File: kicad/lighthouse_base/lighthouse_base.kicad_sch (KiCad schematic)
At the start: 2 parts, among them J1 USB_C_Receptacle_USB2.0_14P, U1 NINA-B312

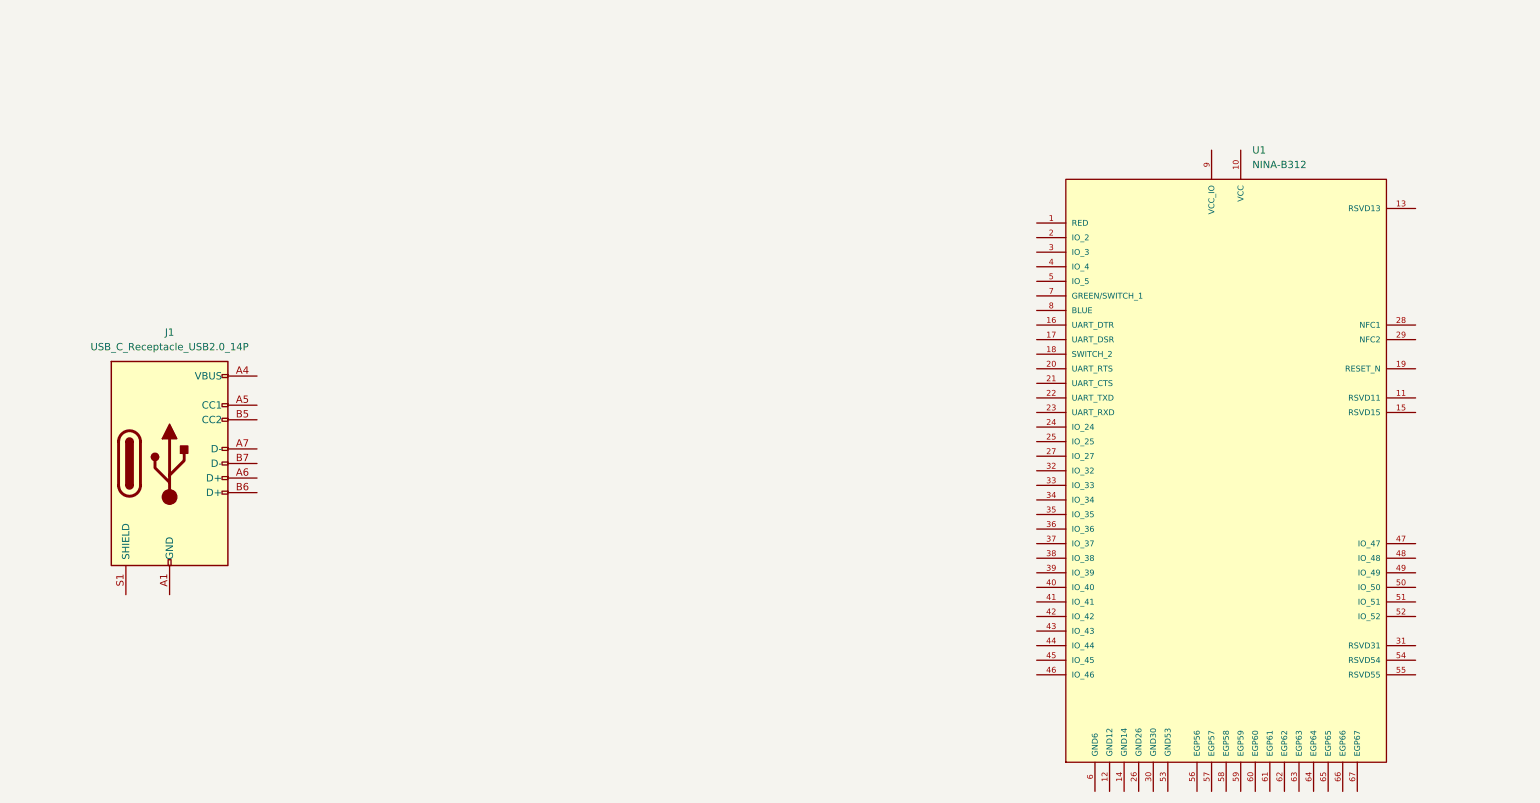
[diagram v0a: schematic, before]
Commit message: added sheets for mcu and peripherials
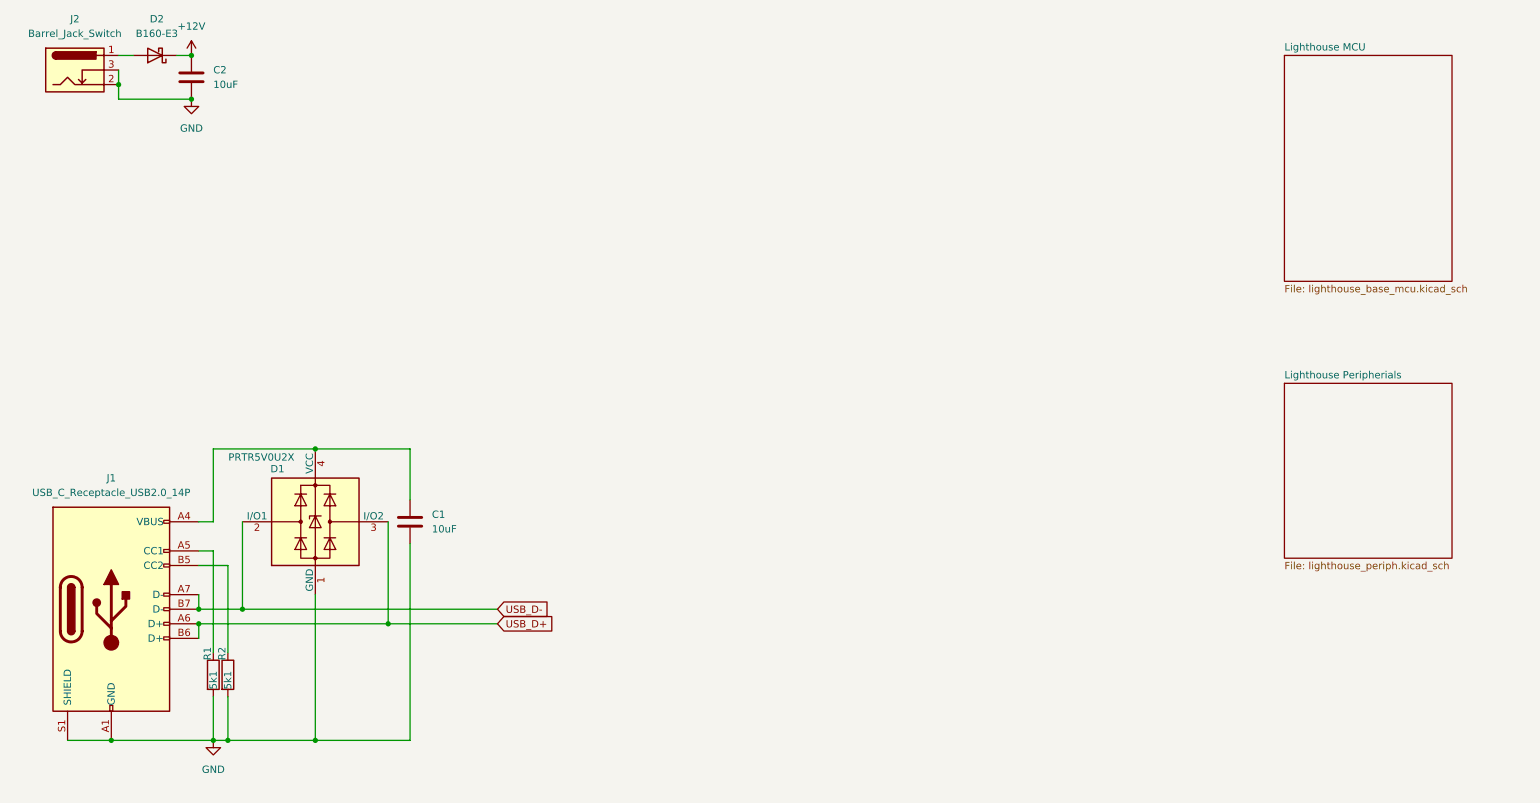
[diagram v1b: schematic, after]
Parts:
- removed U1: NINA-B312, NINA-B312:NINA_LGA67R_1500X1000X338_PIFA, symbol NINA-B312:NINA-B312
- added C1, C2: 10uF, symbol Device:C
- added D1: PRTR5V0U2X, Package_TO_SOT_SMD:SOT-143, symbol Power_Protection:PRTR5V0U2X
- added D2: B160-E3, Diode_SMD:D_SMA, symbol Diode:B160-E3
- added J2: Barrel_Jack_Switch, symbol Connector:Barrel_Jack_Switch
- added R1, R2: 5k1, symbol Device:R
- J1: footprint (none) -> Connector_USB:USB_C_Receptacle_GCT_USB4110
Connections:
- net GND: now reaches J1.A1 (GND), J1.A12 (GND), J1.B1 (GND), J1.B12 (GND)
- net GND: now also J1.S1 (SHIELD), C1.2, C2.2, D1.1 (GND), J2.2, J2.3, R1.2, R2.2
- net at J1.A4 (VBUS), J1.A9 (VBUS), J1.B4 (VBUS)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: now also C1.1, D1.4 (VCC)
- net at J1.A5 (CC1): now also R1.1
- net USB_D+: now reaches J1.A6 (D+)
- net USB_D+: now also J1.B6 (D+), D1.3 (I/O2)
- net USB_D-: now reaches J1.A7 (D-)
- net USB_D-: now also J1.B7 (D-), D1.2 (I/O1)
- net at J1.B5 (CC2): now also R2.1
- new net: D2.2 (A), J2.1
- new net +12V: C2.1, D2.1 (K)
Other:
- added sheet Lighthouse MCU (lighthouse_base_mcu.kicad_sch)
- added sheet Lighthouse Peripherials (lighthouse_periph.kicad_sch)
- moved on the sheet: J1

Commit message: schema v1 done
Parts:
- removed D2: B160-E3, Diode_SMD:D_SMA, symbol Diode:B160-E3
- added C11, C12, C13: 10uF, symbol Device:C
- added D2, D3: B130-13-F, symbol Device:D_Schottky
- added D4: DF2S16FS, Diode_SMD:D_SOD-523, symbol Diode:ESD5Zxx
- added Q1: PMOS, symbol Simulation_SPICE:PMOS
- added R7, R8: 22R, symbol Device:R
- added U6: R-78E5.0-1.0, Converter_DCDC:Converter_DCDC_RECOM_R-78E-0.5_THT, symbol Regulator_Switching:R-78E5.0-1.0
- added U7: TLV75533PDBV, Package_TO_SOT_SMD:SOT-23-5, symbol Regulator_Linear:TLV75533PDBV
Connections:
- net +12V: now also Q1.3 (S), U6.1 (IN)
- net GND: now also C11.2, C12.2, C13.2, D4.2 (A), Q1.2 (G), U6.2 (GND), U7.2 (GND)
- net USB_D+: now also R8.2; no longer D1.3 (I/O2), J1.A6 (D+), J1.B6 (D+)
- net USB_D-: now also R7.2; no longer D1.2 (I/O1), J1.A7 (D-), J1.B7 (D-)
- net VBUS: now reaches C1.1, D1.4 (VCC), J1.A4 (VBUS), J1.A9 (VBUS), J1.B4 (VBUS), J1.B9 (VBUS)
- net VBUS: now also D2.2 (A)
- net at J2.1: now also D4.1 (K), Q1.1 (D)
- new net: D1.3 (I/O2), J1.A6 (D+), J1.B6 (D+), R8.1
- new net: D1.2 (I/O1), J1.A7 (D-), J1.B7 (D-), R7.1
- new net: C12.1, D3.2 (A), U6.3 (OUT)
- new net +3.3V: C13.1, U7.5 (OUT)
- new net +5V: C11.1, D2.1 (K), D3.1 (K), U7.1 (IN), U7.3 (EN)
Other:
- note added: "R-78K5.0-0.5 R-78E5.0-1.0"
- moved on the sheet: C1, C2, D1, J1, J2, R1, R2

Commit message: schematics done
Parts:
- added BT1: Battery_Cell, Connector_PinHeader_2.54mm:PinHeader_1x02_P2.54mm_Vertical, symbol Device:Battery_Cell
- added C6: 10nF, Capacitor_SMD:C_0201_0603Metric_Pad0.64x0.40mm_HandSolder, symbol Device:C
- added R1: 1M, Resistor_SMD:R_0603_1608Metric_Pad0.98x0.95mm_HandSolder, symbol Device:R
- added R2: 10k, Resistor_SMD:R_0603_1608Metric_Pad0.98x0.95mm_HandSolder, symbol Device:R
- added U2: MCP73831-2-OT, Package_TO_SOT_SMD:SOT-23-5, symbol Battery_Management:MCP73831-2-OT
- added U4: MCP111T-xxxE_TT, Package_TO_SOT_SMD:SOT-23-3, symbol MEgliParts:MCP111T-xxxE_TT
- C1: renamed from C2; footprint (none) -> Capacitor_SMD:C_0805_2012Metric_Pad1.18x1.45mm_HandSolder
- C2: renamed from C12; footprint (none) -> Capacitor_SMD:C_0805_2012Metric_Pad1.18x1.45mm_HandSolder
- C3: renamed from C11; footprint (none) -> Capacitor_SMD:C_0805_2012Metric_Pad1.18x1.45mm_HandSolder
- C4: renamed from C13; footprint (none) -> Capacitor_SMD:C_0805_2012Metric_Pad1.18x1.45mm_HandSolder
- C5: renamed from C1; footprint (none) -> Capacitor_SMD:C_0805_2012Metric_Pad1.18x1.45mm_HandSolder
- D1: renamed from D3; footprint (none) -> Diode_SMD:D_SMA_Handsoldering
- D3: renamed from D2; footprint (none) -> Diode_SMD:D_SMA_Handsoldering
- Q1: footprint (none) -> Package_TO_SOT_SMD:SOT-23
- R3: renamed from R7; footprint (none) -> Resistor_SMD:R_0603_1608Metric_Pad0.98x0.95mm_HandSolder
- R4: renamed from R8; footprint (none) -> Resistor_SMD:R_0603_1608Metric_Pad0.98x0.95mm_HandSolder
- R5: renamed from R1; footprint (none) -> Resistor_SMD:R_0603_1608Metric_Pad0.98x0.95mm_HandSolder
- R6: renamed from R2; footprint (none) -> Resistor_SMD:R_0603_1608Metric_Pad0.98x0.95mm_HandSolder
- renumbered D4 to D2, D1 to D4, J2 to J1, J1 to J2, U6 to U1, U7 to U3
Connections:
- net +5V: now also U2.4 (V_{DD}); no longer U3.1 (IN), U3.3 (EN)
- net GND: now also BT1.2 (-), C6.2, R2.2, U2.2 (V_{SS}), U4.2 (VSS)
- new net: C6.1, R1.2, U3.3 (EN), U4.1 (VOUT)
- new net: R2.1, U2.5 (PROG)
- new net +BATT: BT1.1 (+), R1.1, U2.3 (V_{BAT}), U3.1 (IN), U4.3 (VDD)
- new net CH_STAT: U2.1 (STAT)
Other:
- moved on the sheet: C3, C4, U3

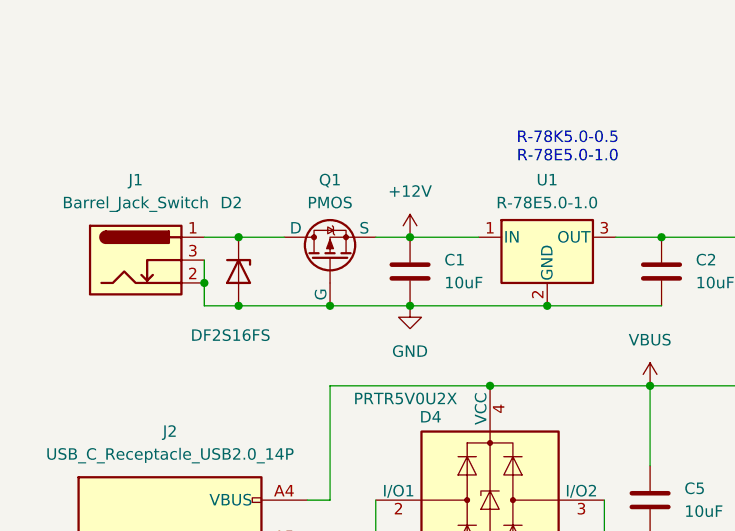
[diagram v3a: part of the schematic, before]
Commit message: started with pcb lighthouse_base
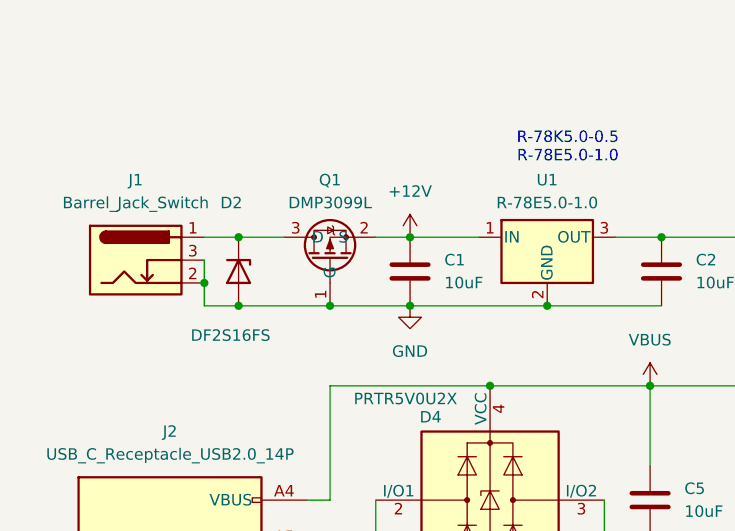
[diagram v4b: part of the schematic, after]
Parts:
- removed Q1: PMOS, Package_TO_SOT_SMD:SOT-23, symbol Simulation_SPICE:PMOS
- added Q1: DMP3099L, Package_TO_SOT_SMD:SOT-23-3, symbol lighthouse1:DMP3099L_PMOSFET
- C6: footprint Capacitor_SMD:C_0201_0603Metric_Pad0.64x0.40mm_HandSolder -> Capacitor_SMD:C_0603_1608Metric_Pad1.08x0.95mm_HandSolder
- J1: footprint (none) -> Connector_BarrelJack:BarrelJack_CUI_PJ-063AH_Horizontal
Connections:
- net +12V: now also Q1.2 (S)
- net GND: now also Q1.1 (G)
- net at D2.1 (K), J1.1: now also Q1.3 (D)

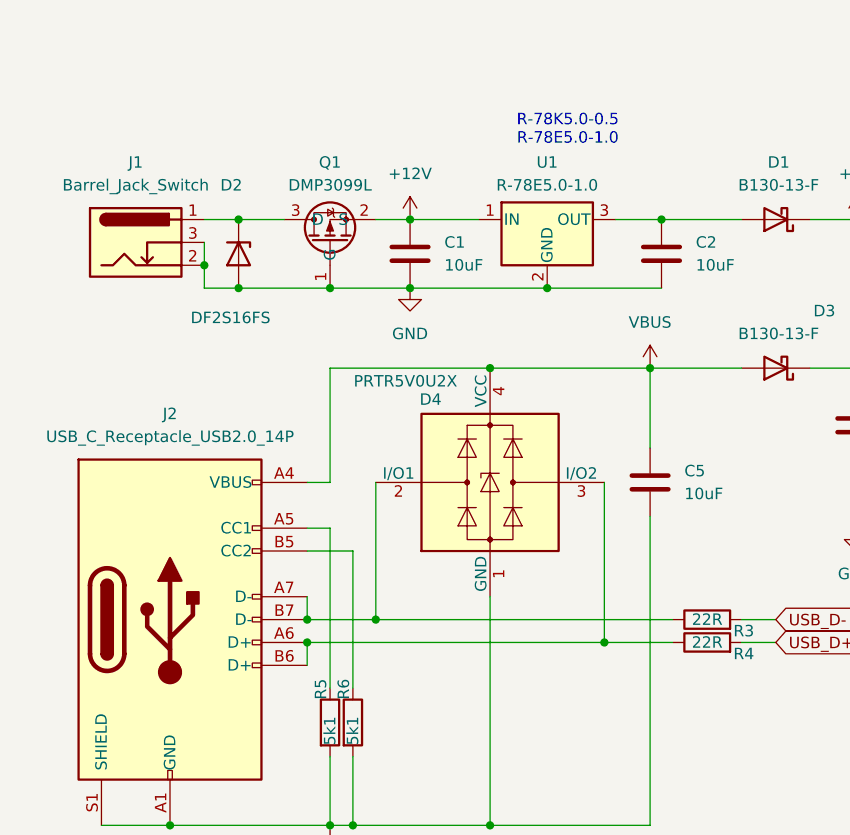
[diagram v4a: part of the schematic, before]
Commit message: rev1: added 32 kHz XTAL, interrupt signals for VBUS + +5V, ... many more
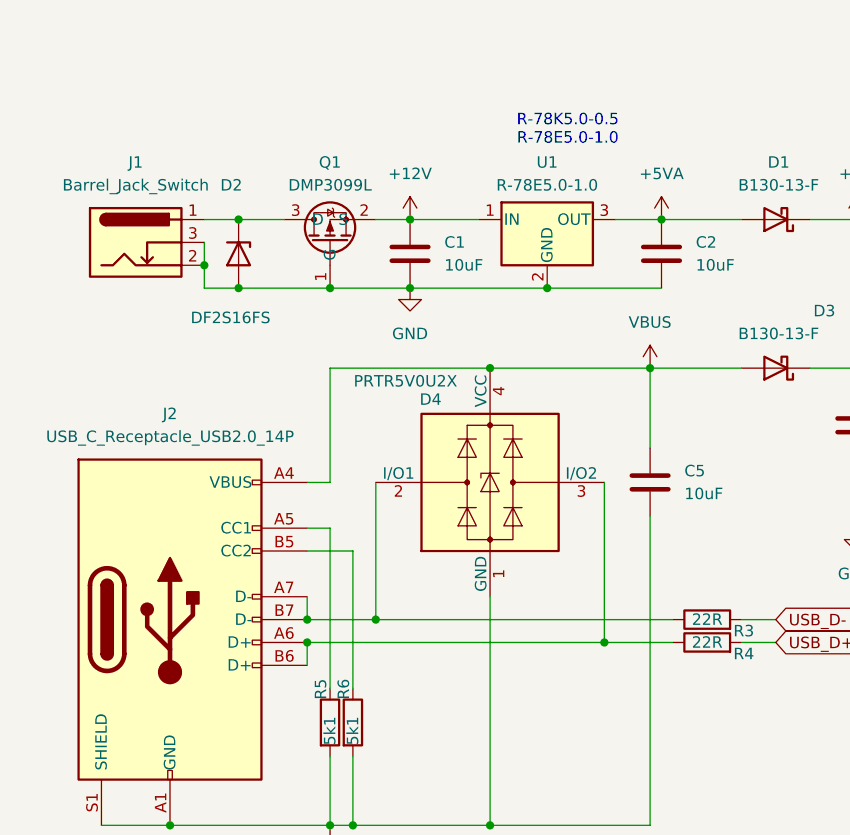
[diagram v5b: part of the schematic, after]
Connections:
- net +5VA: now reaches C2.1, D1.2 (A), U1.3 (OUT)
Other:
- title: (none) -> Lighthouse Base
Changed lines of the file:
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@@
 (kicad_sch
-	(version 20231120)
+	(version 20250114)
 	(generator "eeschema")
-	(generator_version "8.0")
+	(generator_version "9.0")
 	(paper "A4")
+	(title_block
+		(title "Lighthouse Base")
+		(date "2025-09-28")
+		(rev "1")
+		(comment 1 "MEgli")
+	)
+	(text "R-78K5.0-0.5\nR-78E5.0-1.0"
+		(exclude_from_sim no)
+		(at 79.756 37.084 0)
+		(effects
+			(font
+				(size 1.27 1.27)
+			)
+		)
+	)
 	(junction
 		(at 88.9 63.5)
@@
 		)
 	)
-	(text "R-78K5.0-0.5\nR-78E5.0-1.0"
-		(exclude_from_sim no)
-		(at 79.756 37.084 0)
-		(effects
-			(font
-				(size 1.27 1.27)
-			)
-		)
-	)
 	(global_label "USB_D-"
 		(shape input)
@@
 	)
 	(symbol
+		(lib_id "power:+5VA")
+		(at 90.17 46.99 0)
+		(unit 1)
+		(exclude_from_sim no)
+		(in_bom yes)
+		(on_board yes)
+		(dnp no)
+		(fields_autoplaced yes)
+		(property "Reference" "#PWR039"
+			(at 90.17 50.8 0)
+			(effects
+				(font
+					(size 1.27 1.27)
+				)
+				(hide yes)
+			)
+		)
+		(property "Value" "+5VA"
+			(at 90.17 41.91 0)
+			(effects
+				(font
+					(size 1.27 1.27)
+				)
+			)
+		)
+		(property "Footprint" ""
+			(at 90.17 46.99 0)
+			(effects
+				(font
+					(size 1.27 1.27)
+				)
+				(hide yes)
+			)
+		)
+		(property "Datasheet" ""
+			(at 90.17 46.99 0)
+			(effects
+				(font
+					(size 1.27 1.27)
+				)
+				(hide yes)
+			)
+		)
+		(property "Description" "Power symbol creates a global label with name \"+5VA\""
+			(at 90.17 46.99 0)
+			(effects
+				(font
+					(size 1.27 1.27)
+				)
+				(hide yes)
+			)
+		)
+		(pin "1"
+		)
+		(instances
+			(project ""
+				(path "/e329df4a-6588-455a-9936-c9675a4aa830"
+					(reference "#PWR039")
+					(unit 1)
+				)
+			)
+		)
+	)
+	(symbol
 		(lib_id "Device:Battery_Cell")
 		(at 149.86 73.66 0)
@@
 		(at 240.03 82.55)
 		(size 29.21 30.48)
+		(exclude_from_sim no)
+		(in_bom yes)
+		(on_board yes)
+		(dnp no)
 		(fields_autoplaced yes)
 		(stroke
@@
 		(at 240.03 25.4)
 		(size 29.21 39.37)
+		(exclude_from_sim no)
+		(in_bom yes)
+		(on_board yes)
+		(dnp no)
 		(fields_autoplaced yes)
 		(stroke
@@
 		)
 	)
+	(embedded_fonts no)
 )
